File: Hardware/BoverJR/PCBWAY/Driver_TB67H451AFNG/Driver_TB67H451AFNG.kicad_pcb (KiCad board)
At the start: 2 copper layers, 25 x 25 mm, 8 parts, among them J1 POWER, J3 MOTOR, J4 Conn_01x04_Pin, U1 TB67H451AFNG

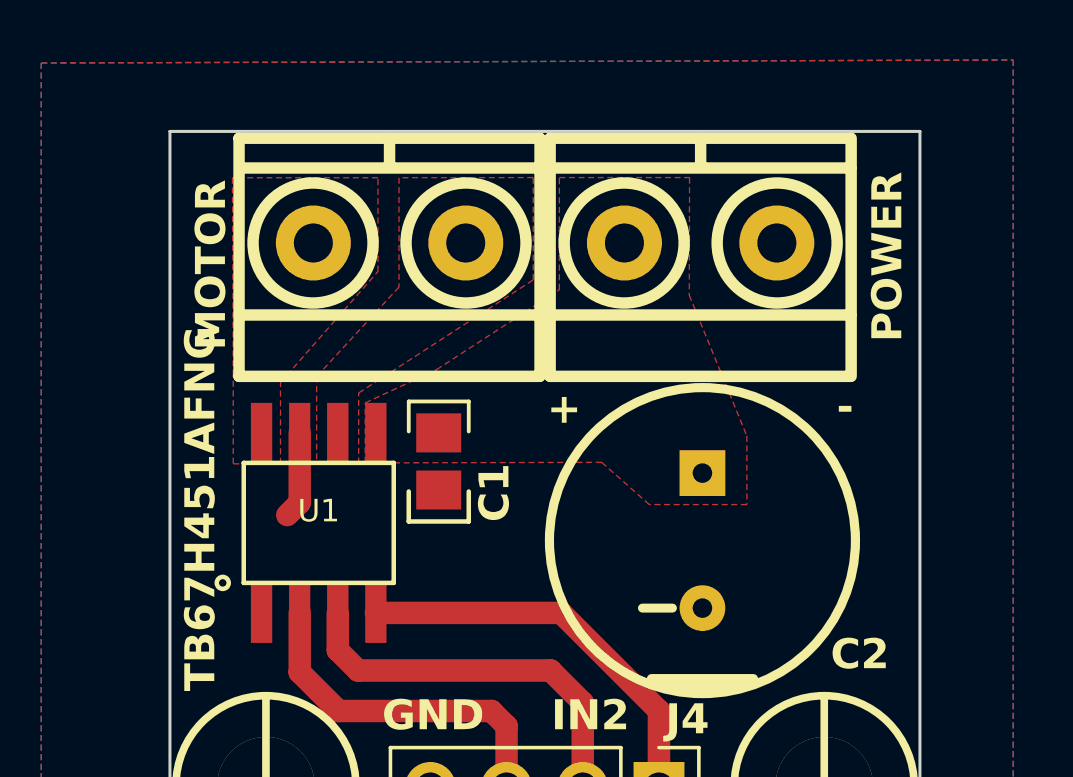
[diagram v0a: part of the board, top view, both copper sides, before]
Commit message: Rediseño Driver TB67
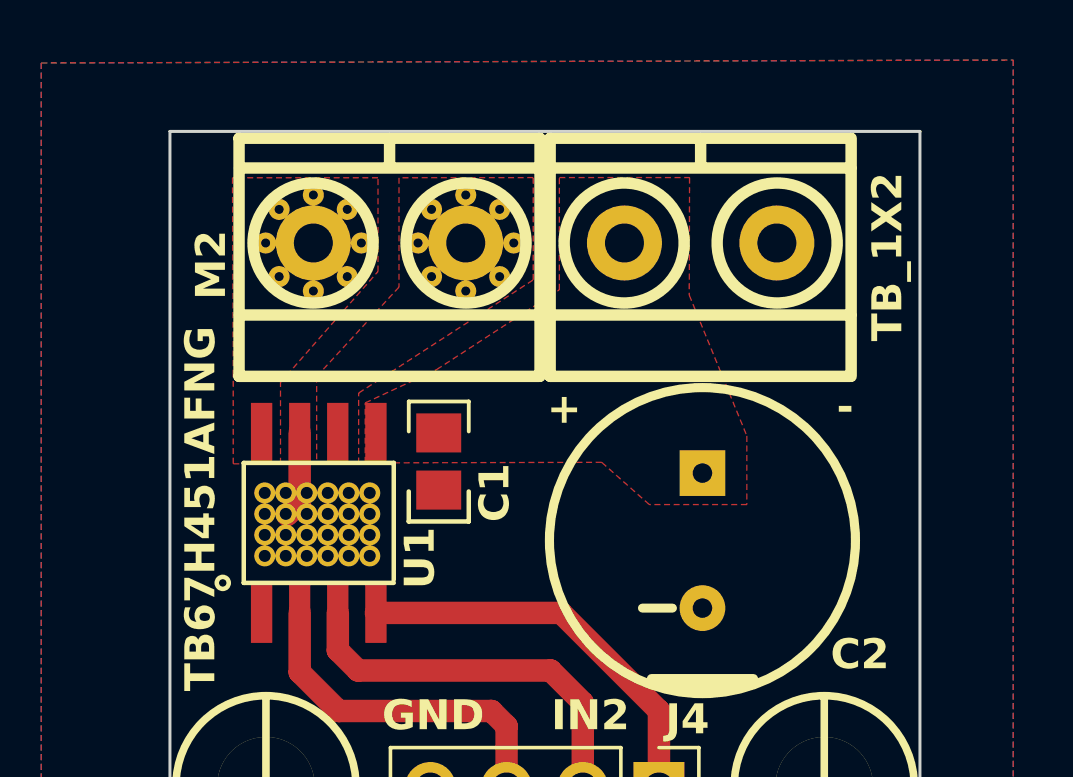
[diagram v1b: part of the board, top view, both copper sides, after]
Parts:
- J1: value POWER -> TB_1X2
- J3: value MOTOR -> M2; footprint EESTN5-v2:BORNERA2_AZUL -> EESTN5-v2:BORNERA2_AZUL_HOLES+
- U1: footprint EESTN5-v2:SSOP-8 -> EESTN5-v2:SSOP-8_disipa

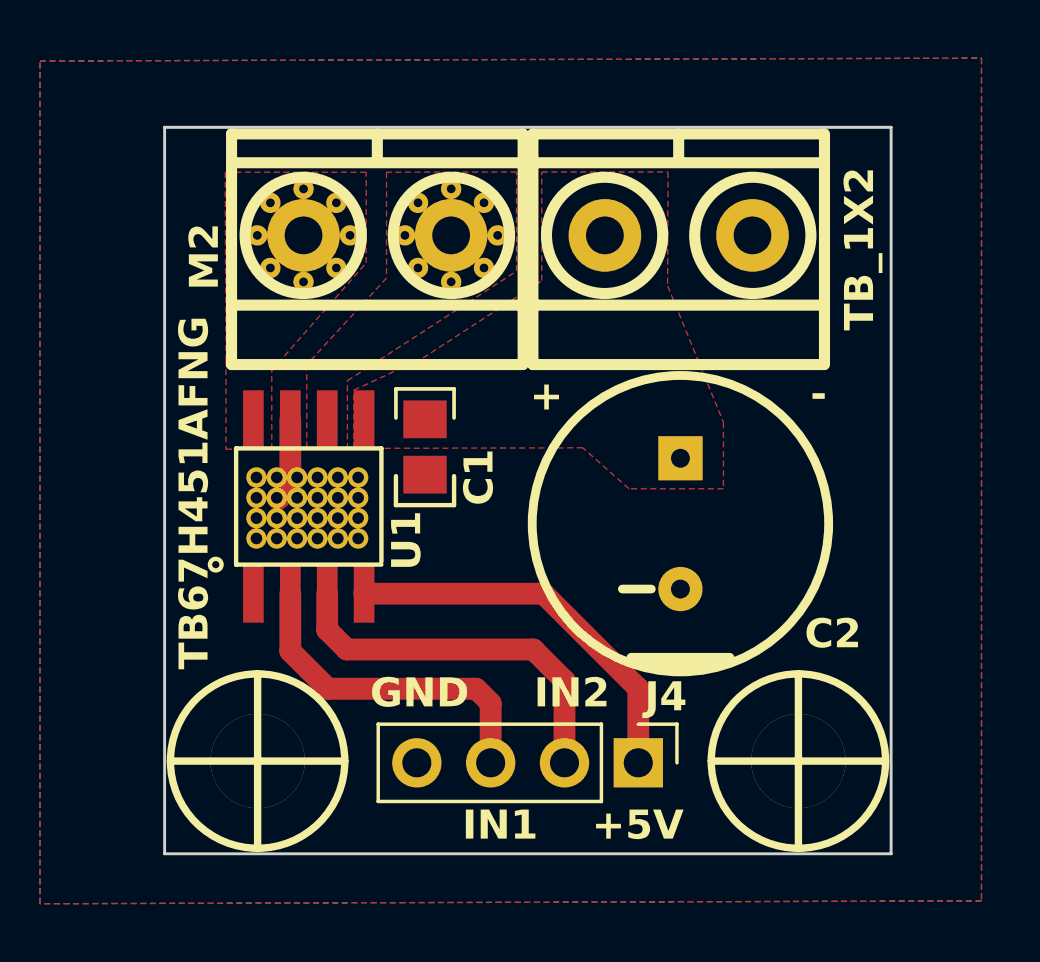
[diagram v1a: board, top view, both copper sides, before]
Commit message: Edicion Driver TB67
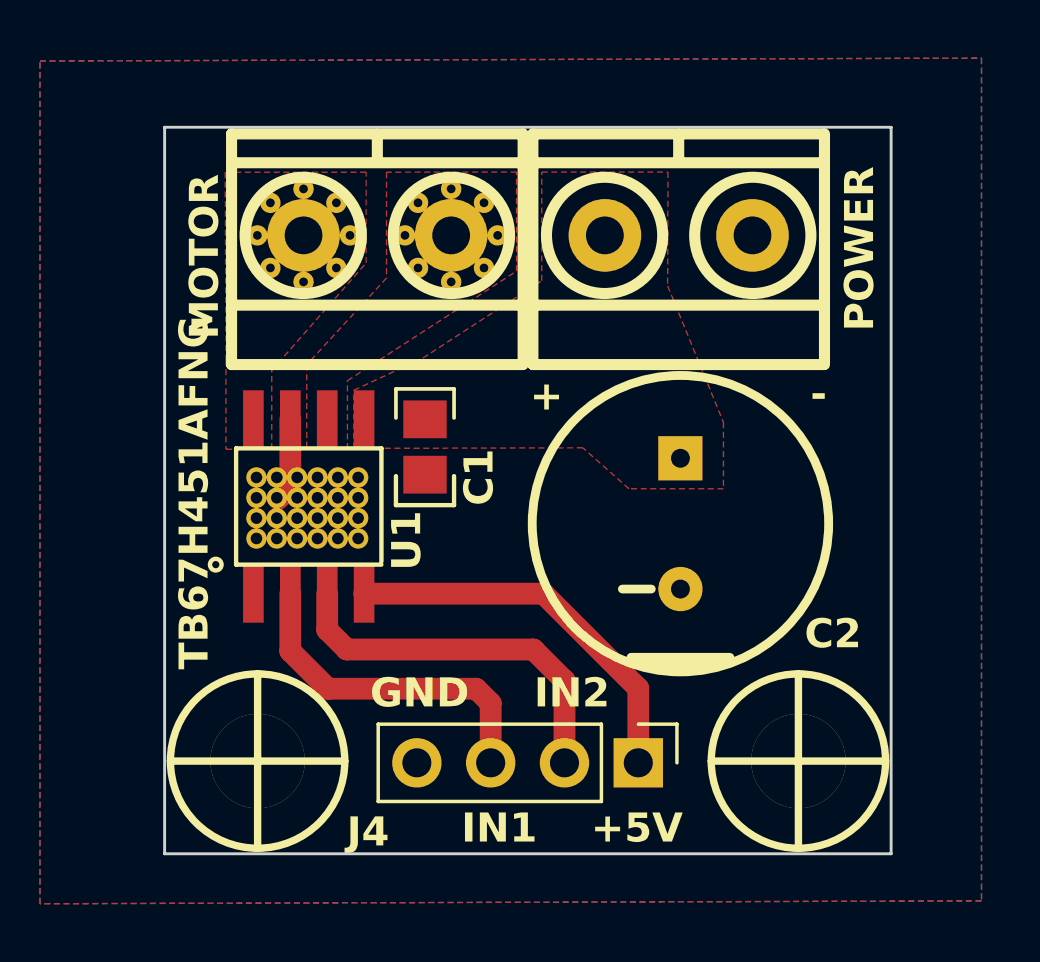
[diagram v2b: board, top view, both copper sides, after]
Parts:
- J1: value TB_1X2 -> POWER
- J3: value M2 -> MOTOR
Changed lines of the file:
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@@
         (effects (font (size 1.5 1.5) (thickness 0.3)))
     )
-    (fp_text value "TB_1X2" (at -6.225 -0.46 90) (layer "F.SilkS")
+    (fp_text value "POWER" (at -6.225 -0.46 90) (layer "F.SilkS")
         (effects (font (size 1 1) (thickness 0.25) bold))
     )
@@
     (property "ki_keywords" "connector")
     (attr through_hole)
-    (fp_text reference "J4" (at -2.27 -0.95 180) (layer "F.SilkS")
+    (fp_text reference "J4" (at 2.38 9.3 180) (layer "F.SilkS")
         (effects (font (size 1 1) (thickness 0.25) bold))
     )
@@
         (effects (font (size 1.5 1.5) (thickness 0.3)))
     )
-    (fp_text value "M2" (at 5.95 -0.73 90) (layer "F.SilkS")
+    (fp_text value "MOTOR" (at 5.95 -0.73 90) (layer "F.SilkS")
         (effects (font (size 1 1) (thickness 0.25) bold))
     )
@@
     (effects (font (size 1 1) (thickness 0.25) bold) (justify left bottom))
   )
-  (gr_text "IN1\n" (at 155.53 110.88) (layer "F.SilkS")
+  (gr_text "IN1\n" (at 155.5 110.98) (layer "F.SilkS")
     (effects (font (size 1 1) (thickness 0.25) bold) (justify left bottom))
   )
-  (gr_text "+5V" (at 159.99 110.88) (layer "F.SilkS")
+  (gr_text "+5V" (at 159.96 110.98) (layer "F.SilkS")
     (effects (font (size 1 1) (thickness 0.25) bold) (justify left bottom))
   )

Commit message: cambios gerber
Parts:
- moved C1 25.1 mm to (140.2, 118.0)
- moved C2 25.1 mm to (148.9, 120.6)
- moved H1 25.1 mm to (134.4, 128.8)
- moved H2 25.1 mm to (153.0, 128.8)
- moved J1 25.1 mm to (148.9, 110.7)
- moved J3 25.1 mm to (138.5, 110.7)
- moved J4 25.1 mm to (147.5, 128.9)
- moved U1 25.1 mm to (136.2, 120.0)
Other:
- outline, holes or cut-outs redrawn
